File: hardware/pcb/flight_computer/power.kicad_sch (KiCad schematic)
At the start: 31 parts, among them U2 TPS563201DDCR, U3 TPS73633DRBR, U7 AZ1117-5.0

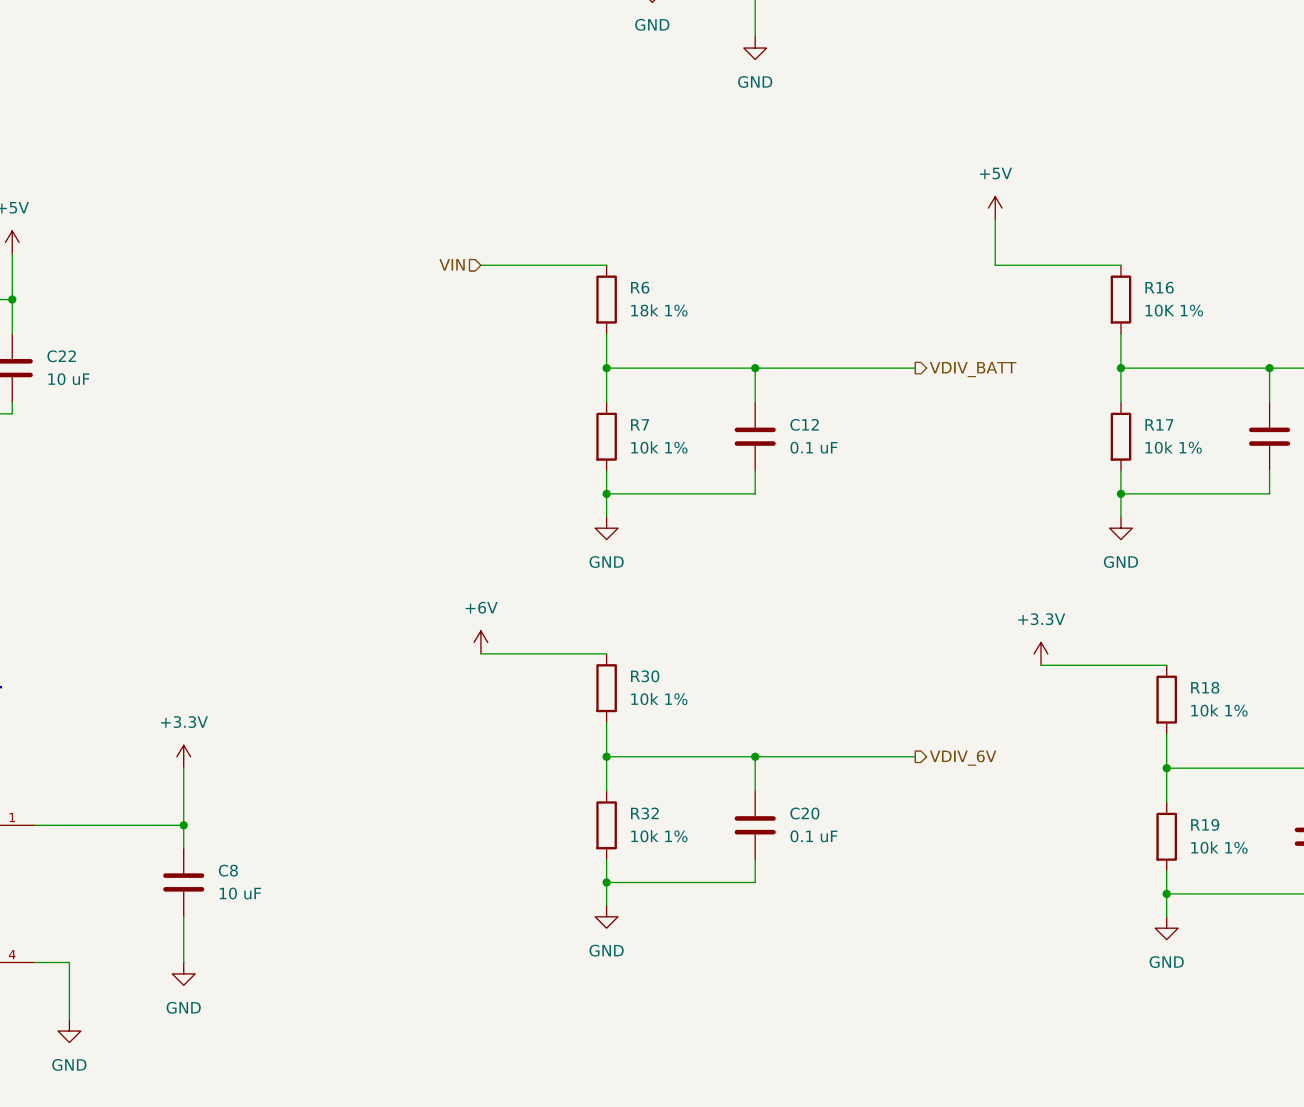
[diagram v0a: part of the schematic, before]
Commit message: Added 3D model
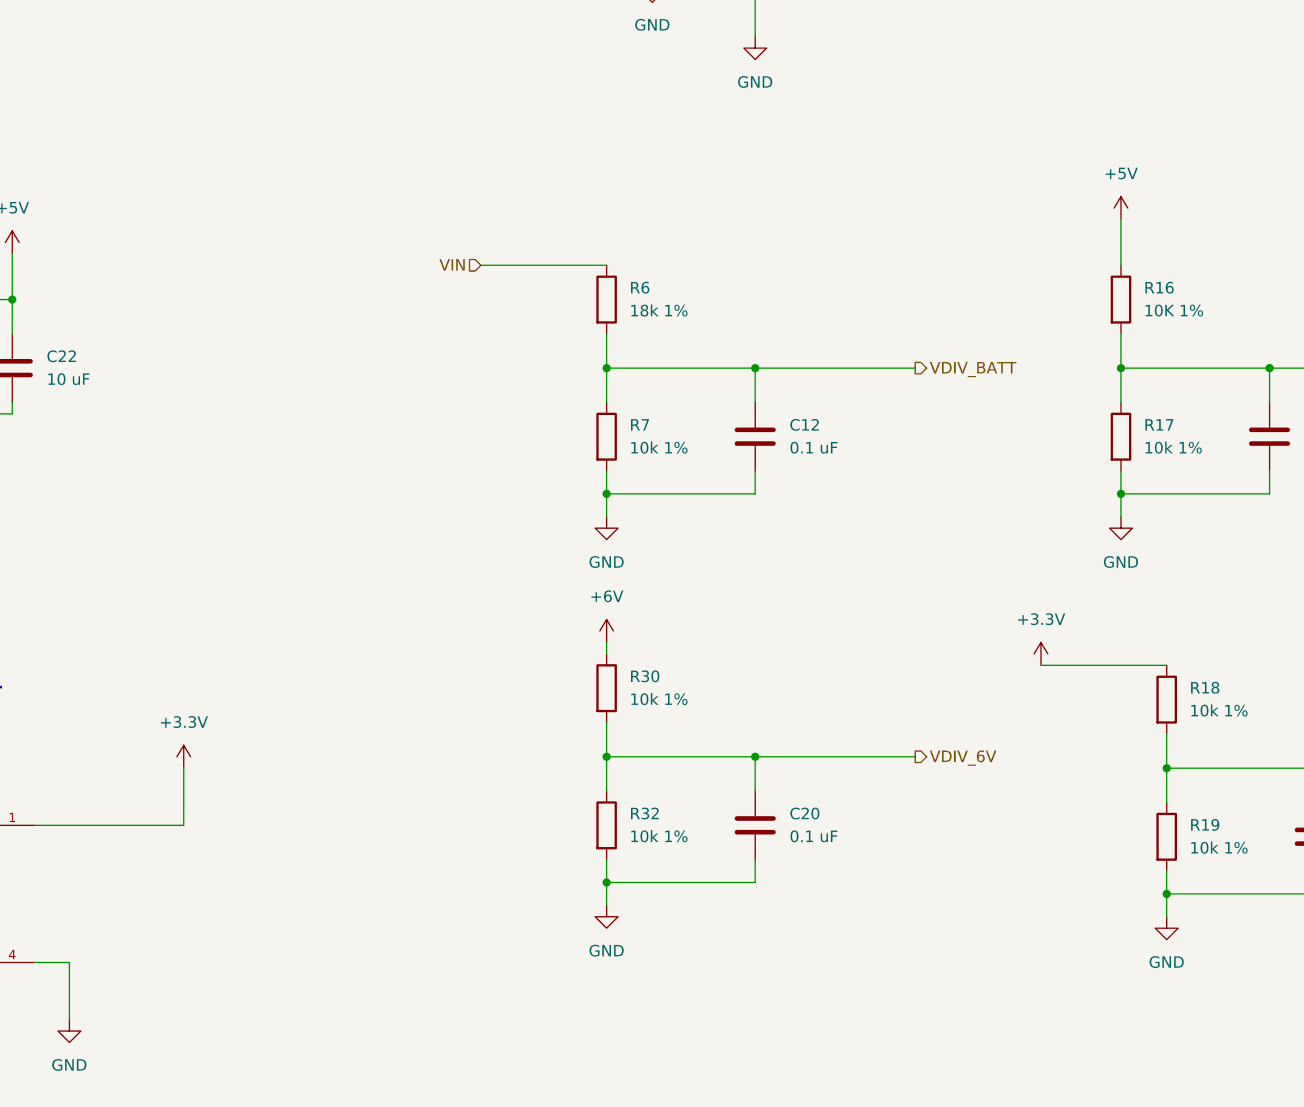
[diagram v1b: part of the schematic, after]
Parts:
- removed C8: 10 uF, Capacitor_SMD:C_0603_1608Metric, symbol Device:C
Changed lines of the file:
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@@
 	)
 	(junction
-		(at 110.49 148.59)
-		(diameter 0)
-		(color 0 0 0 0)
-	)
-	(junction
 		(at 91.44 90.17)
 		(diameter 0)
@@
 	(wire
 		(pts
-			(xy 200.66 86.36) (xy 214.63 86.36)
-		)
-		(stroke
-			(width 0)
-			(type default)
-		)
-	)
-	(wire
-		(pts
 			(xy 180.34 30.48) (xy 180.34 31.75)
 		)
@@
 	(wire
 		(pts
-			(xy 143.51 129.54) (xy 157.48 129.54)
-		)
-		(stroke
-			(width 0)
-			(type default)
-		)
-	)
-	(wire
-		(pts
 			(xy 173.99 152.4) (xy 173.99 154.94)
 		)
@@
 	(wire
 		(pts
+			(xy 157.48 128.27) (xy 157.48 129.54)
+		)
+		(stroke
+			(width 0)
+			(type default)
+		)
+	)
+	(wire
+		(pts
 			(xy 219.71 153.67) (xy 219.71 156.21)
 		)
@@
 	(wire
 		(pts
-			(xy 110.49 158.75) (xy 110.49 163.83)
-		)
-		(stroke
-			(width 0)
-			(type default)
-		)
-	)
-	(wire
-		(pts
 			(xy 110.49 142.24) (xy 110.49 148.59)
 		)
@@
 	(wire
 		(pts
-			(xy 200.66 81.28) (xy 200.66 86.36)
+			(xy 214.63 81.28) (xy 214.63 86.36)
 		)
 		(stroke
@@
 	(wire
 		(pts
-			(xy 110.49 148.59) (xy 110.49 151.13)
-		)
-		(stroke
-			(width 0)
-			(type default)
-		)
-	)
-	(wire
-		(pts
 			(xy 53.34 102.87) (xy 72.39 102.87)
 		)
@@
 	(symbol
 		(lib_id "power:+5V")
-		(at 200.66 81.28 0)
+		(at 214.63 81.28 0)
 		(unit 1)
 		(body_style 1)
@@
 		(fields_autoplaced yes)
 		(property "Reference" "#PWR042"
-			(at 200.66 85.09 0)
+			(at 214.63 85.09 0)
 			(hide yes)
 			(show_name no)
@@
 		)
 		(property "Value" "+5V"
-			(at 200.66 76.2 0)
+			(at 214.63 76.2 0)
 			(show_name no)
 			(do_not_autoplace no)
@@
 		)
 		(property "Footprint" ""
-			(at 200.66 81.28 0)
+			(at 214.63 81.28 0)
 			(hide yes)
 			(show_name no)
@@
 		)
 		(property "Datasheet" ""
-			(at 200.66 81.28 0)
+			(at 214.63 81.28 0)
 			(hide yes)
 			(show_name no)
@@
 		)
 		(property "Description" "Power symbol creates a global label with name \"+5V\""
-			(at 200.66 81.28 0)
+			(at 214.63 81.28 0)
 			(hide yes)
 			(show_name no)
@@
 	)
 	(symbol
-		(lib_id "Device:C")
-		(at 110.49 154.94 0)
-		(unit 1)
-		(body_style 1)
-		(exclude_from_sim no)
-		(in_bom yes)
-		(on_board yes)
-		(in_pos_files yes)
-		(dnp no)
-		(fields_autoplaced yes)
-		(property "Reference" "C8"
-			(at 114.3 153.6699 0)
-			(show_name no)
-			(do_not_autoplace no)
-			(effects
-				(font
-					(size 1.27 1.27)
-				)
-				(justify left)
-			)
-		)
-		(property "Value" "10 uF"
-			(at 114.3 156.2099 0)
-			(show_name no)
-			(do_not_autoplace no)
-			(effects
-				(font
-					(size 1.27 1.27)
-				)
-				(justify left)
-			)
-		)
-		(property "Footprint" "Capacitor_SMD:C_0603_1608Metric"
-			(at 111.4552 158.75 0)
-			(hide yes)
-			(show_name no)
-			(do_not_autoplace no)
-			(effects
-				(font
-					(size 1.27 1.27)
-				)
-			)
-		)
-		(property "Datasheet" ""
-			(at 110.49 154.94 0)
-			(hide yes)
-			(show_name no)
-			(do_not_autoplace no)
-			(effects
-				(font
-					(size 1.27 1.27)
-				)
-			)
-		)
-		(property "Description" "Unpolarized capacitor"
-			(at 110.49 154.94 0)
-			(hide yes)
-			(show_name no)
-			(do_not_autoplace no)
-			(effects
-				(font
-					(size 1.27 1.27)
-				)
-			)
-		)
-		(pin "2"
-		)
-		(pin "1"
-		)
-		(instances
-			(project "flight_computer"
-				(path "/97739cb3-517e-4f70-8350-1cb198e6b8e6/969565cd-9cbf-402f-9456-10bb21147adc"
-					(reference "C8")
-					(unit 1)
-				)
-			)
-		)
-	)
-	(symbol
 		(lib_id "Device:R")
 		(at 214.63 105.41 0)
@@
 	(symbol
 		(lib_id "power:+5V")
-		(at 143.51 129.54 0)
+		(at 157.48 128.27 0)
 		(unit 1)
 		(body_style 1)
@@
 		(fields_autoplaced yes)
 		(property "Reference" "#PWR056"
-			(at 143.51 133.35 0)
+			(at 157.48 132.08 0)
 			(hide yes)
 			(show_name no)
@@
 		)
 		(property "Value" "+6V"
-			(at 143.51 124.46 0)
+			(at 157.48 123.19 0)
 			(show_name no)
 			(do_not_autoplace no)
@@
 		)
 		(property "Footprint" ""
-			(at 143.51 129.54 0)
+			(at 157.48 128.27 0)
 			(hide yes)
 			(show_name no)
@@
 		)
 		(property "Datasheet" ""
-			(at 143.51 129.54 0)
+			(at 157.48 128.27 0)
 			(hide yes)
 			(show_name no)
@@
 		)
 		(property "Description" "Power symbol creates a global label with name \"+5V\""
-			(at 143.51 129.54 0)
+			(at 157.48 128.27 0)
 			(hide yes)
 			(show_name no)
@@
 					(unit 1)
 				)
-			)
-		)
-	)
-	(symbol
-		(lib_id "power:GND")
-		(at 110.49 163.83 0)
-		(unit 1)
-		(body_style 1)
-		(exclude_from_sim no)
-		(in_bom yes)
-		(on_board yes)
-		(in_pos_files yes)
-		(dnp no)
-		(fields_autoplaced yes)
-		(property "Reference" "#PWR012"
-			(at 110.49 170.18 0)
-			(hide yes)
-			(show_name no)
-			(do_not_autoplace no)
-			(effects
-				(font
-					(size 1.27 1.27)
-				)
-			)
-		)
-		(property "Value" "GND"
-			(at 110.49 168.91 0)
-			(show_name no)
-			(do_not_autoplace no)
-			(effects
-				(font
-					(size 1.27 1.27)
-				)
-			)
-		)
-		(property "Footprint" ""
-			(at 110.49 163.83 0)
-			(hide yes)
-			(show_name no)
-			(do_not_autoplace no)
-			(effects
-				(font
-					(size 1.27 1.27)
-				)
-			)
-		)
-		(property "Datasheet" ""
-			(at 110.49 163.83 0)
-			(hide yes)
-			(show_name no)
-			(do_not_autoplace no)
-			(effects
-				(font
-					(size 1.27 1.27)
-				)
-			)
-		)
-		(property "Description" "Power symbol creates a global label with name \"GND\" , ground"
-			(at 110.49 163.83 0)
-			(hide yes)
-			(show_name no)
-			(do_not_autoplace no)
-			(effects
-				(font
-					(size 1.27 1.27)
-				)
-			)
-		)
-		(pin "1"
-		)
-		(instances
-			(project "flight_computer"
-				(path "/97739cb3-517e-4f70-8350-1cb198e6b8e6/969565cd-9cbf-402f-9456-10bb21147adc"
-					(reference "#PWR012")
-					(unit 1)
-				)
